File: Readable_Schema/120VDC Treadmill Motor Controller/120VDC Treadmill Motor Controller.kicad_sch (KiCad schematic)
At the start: 0 parts

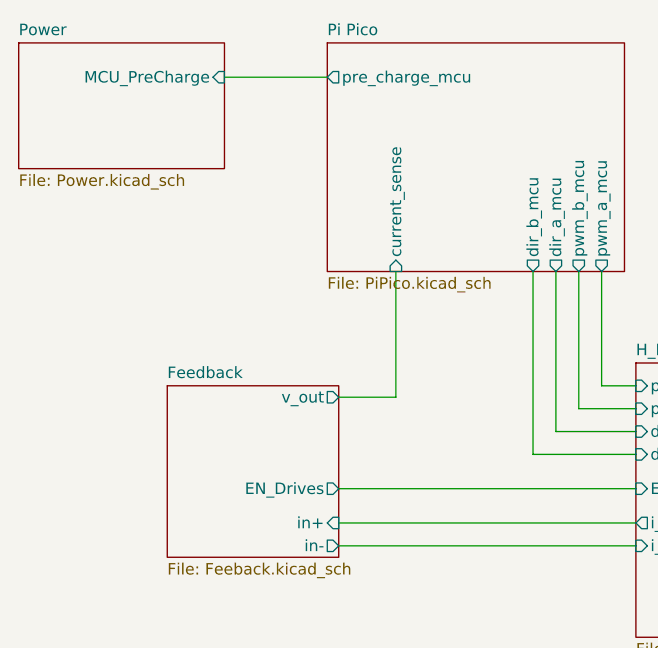
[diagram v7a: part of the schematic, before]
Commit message: -Added voltage sense
-Need to add some kind of LED to tell that the board is HOT

-Need to work with ross to understand the DNMOS setup
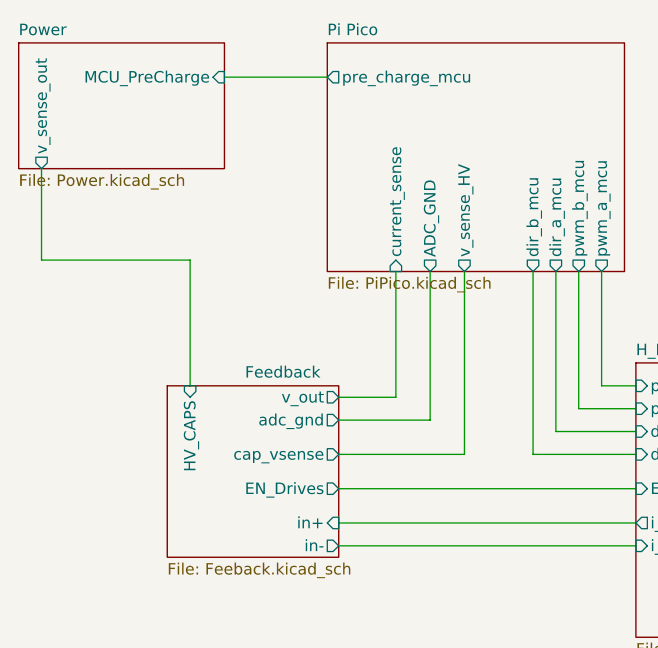
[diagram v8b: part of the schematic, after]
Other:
- sheet Feedback ports: added HV_CAPS, adc_gnd, cap_vsense; removed none
- sheet Pi Pico ports: added ADC_GND, v_sense_HV; removed none
- sheet Power ports: added v_sense_out; removed none
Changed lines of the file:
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@@
+	(wire
+		(pts
+			(xy 123.19 100.33) (xy 133.35 100.33)
+		)
+		(stroke
+			(width 0)
+			(type default)
+		)
+	)
+	(wire
+		(pts
+			(xy 106.68 82.55) (xy 90.17 82.55)
+		)
+		(stroke
+			(width 0)
+			(type default)
+		)
+	)
 	(wire
 		(pts
@@
 	(wire
 		(pts
+			(xy 106.68 96.52) (xy 106.68 82.55)
+		)
+		(stroke
+			(width 0)
+			(type default)
+		)
+	)
+	(wire
+		(pts
+			(xy 137.16 83.82) (xy 137.16 104.14)
+		)
+		(stroke
+			(width 0)
+			(type default)
+		)
+	)
+	(wire
+		(pts
+			(xy 133.35 100.33) (xy 133.35 83.82)
+		)
+		(stroke
+			(width 0)
+			(type default)
+		)
+	)
+	(wire
+		(pts
 			(xy 152.4 83.82) (xy 152.4 96.52)
 		)
@@
 	(wire
 		(pts
+			(xy 90.17 82.55) (xy 90.17 72.39)
+		)
+		(stroke
+			(width 0)
+			(type default)
+		)
+	)
+	(wire
+		(pts
 			(xy 144.78 83.82) (xy 144.78 104.14)
 		)
@@
 		(pts
 			(xy 123.19 111.76) (xy 156.21 111.76)
+		)
+		(stroke
+			(width 0)
+			(type default)
+		)
+	)
+	(wire
+		(pts
+			(xy 137.16 104.14) (xy 123.19 104.14)
 		)
 		(stroke
@@
 			)
 		)
+		(pin "v_sense_out" output
+			(at 90.17 72.39 270)
+			(effects
+				(font
+					(size 1.27 1.27)
+				)
+				(justify left)
+			)
+		)
 		(instances
 			(project "120VDC Treadmill Motor Controller"
@@
 		(on_board yes)
 		(dnp no)
-		(fields_autoplaced yes)
 		(stroke
 			(width 0.1524)
@@
 		)
 		(property "Sheetname" "Feedback"
-			(at 104.14 95.8084 0)
+			(at 112.776 95.758 0)
 			(effects
 				(font
@@
 		(pin "EN_Drives" output
 			(at 123.19 107.95 0)
+			(effects
+				(font
+					(size 1.27 1.27)
+				)
+				(justify right)
+			)
+		)
+		(pin "adc_gnd" output
+			(at 123.19 100.33 0)
+			(effects
+				(font
+					(size 1.27 1.27)
+				)
+				(justify right)
+			)
+		)
+		(pin "cap_vsense" output
+			(at 123.19 104.14 0)
+			(effects
+				(font
+					(size 1.27 1.27)
+				)
+				(justify right)
+			)
+		)
+		(pin "HV_CAPS" input
+			(at 106.68 96.52 90)
 			(effects
 				(font
@@
 			(effects
 				(font
+					(size 1.27 1.27)
+				)
+				(justify left)
+			)
+		)
+		(pin "ADC_GND" output
+			(at 133.35 83.82 270)
+			(effects
+				(font
+					(size 1.27 1.27)
+				)
+				(justify left)
+			)
+		)
+		(pin "v_sense_HV" output
+			(at 137.16 83.82 270)
+			(effects
+				(font
